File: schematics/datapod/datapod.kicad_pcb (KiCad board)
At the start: 2 copper layers, 152.7 x 152.7 mm, 56 parts, among them J1 Conn_01x02, J2 Conn_02x03_Odd_Even, J3 Conn_01x02, J4 DB9_Female, J5 DB9_Male_MountingHoles, J6 Micro_SD_Card, J7 Conn_02x02_Odd_Even, J8 Conn_01x02_Female, K1 DS2E-SL2-DC5V, K2 DS2E-SL2-DC5V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

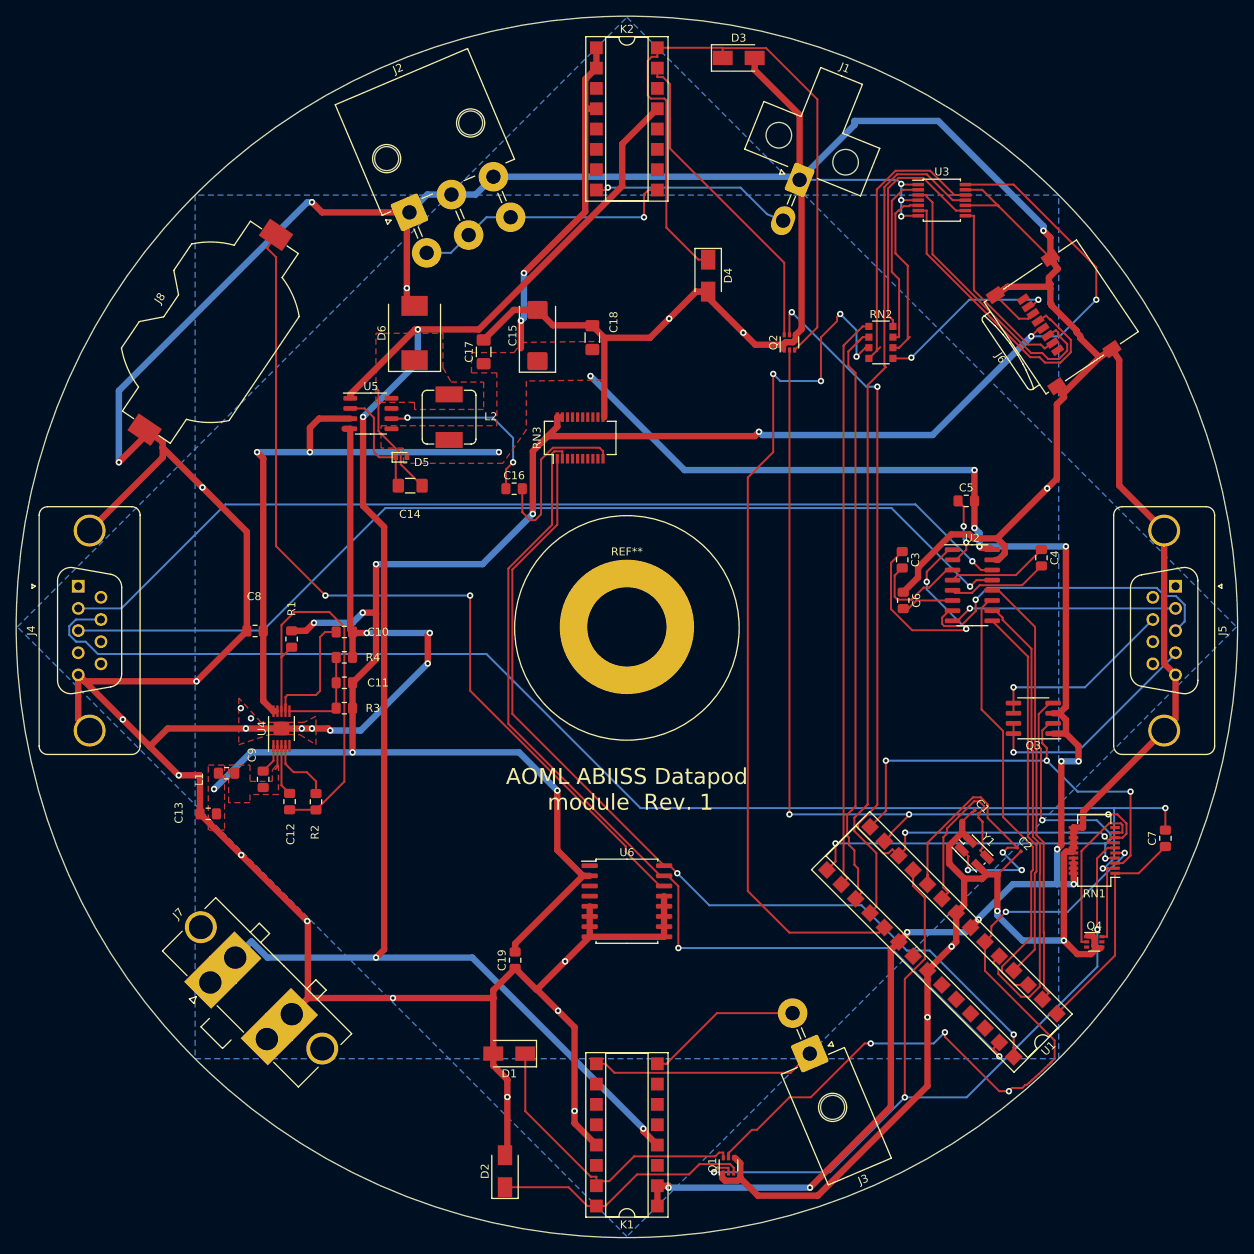
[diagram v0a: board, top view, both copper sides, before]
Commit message: restored lost changes... moving sd card reader and replacing rn2 with actual resistors
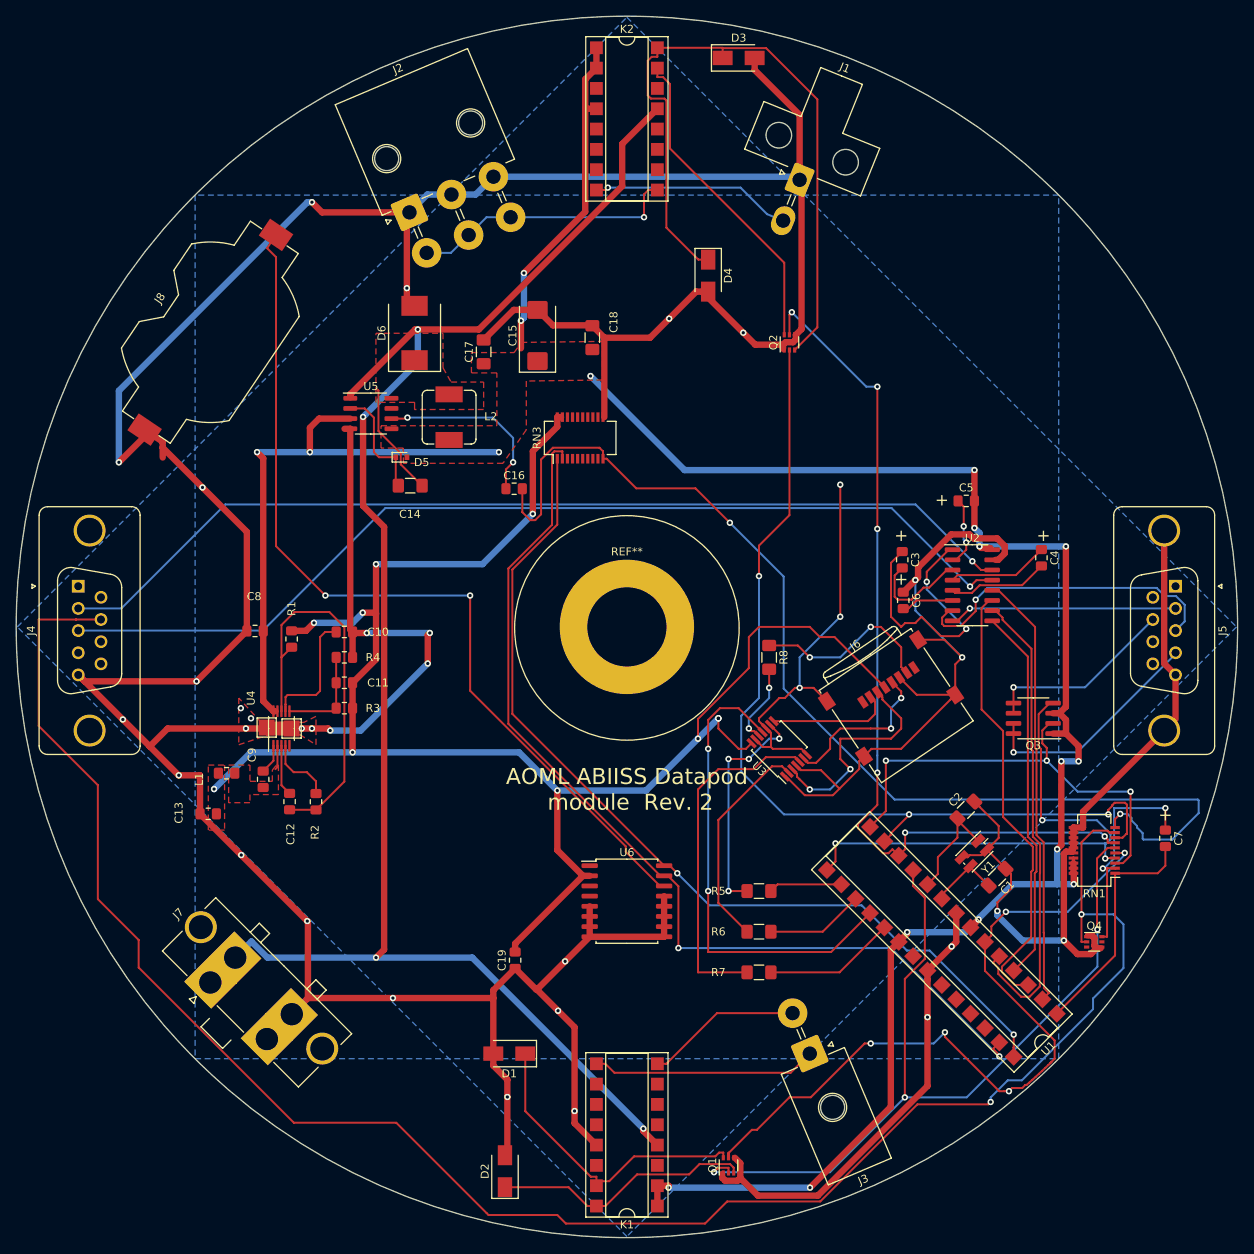
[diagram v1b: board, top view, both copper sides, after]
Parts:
- removed RN2: 3.3K, Resistor_SMD:R_Array_Convex_4x1206
- added R5: 3.3K, Resistor_SMD:R_1206_3216Metric_Pad1.42x1.75mm_HandSolder, F.Cu at (116.8, 129.5)
- added R6: 3.3K, Resistor_SMD:R_1206_3216Metric_Pad1.42x1.75mm_HandSolder, F.Cu at (116.8, 134.6)
- added R7: 3.3K, Resistor_SMD:R_1206_3216Metric_Pad1.42x1.75mm_HandSolder, F.Cu at (116.8, 139.7)
- added R8: 3.3K, Resistor_SMD:R_1206_3216Metric_Pad1.42x1.75mm_HandSolder, F.Cu at (118.1, 100.3)
- added REF**: TestPoint_Pad_2.0x2.0mm, TestPoint:TestPoint_Pad_2.0x2.0mm, F.Cu at (58.4, 109.2)
- added REF**: TestPoint_Pad_2.0x2.0mm, TestPoint:TestPoint_Pad_2.0x2.0mm, F.Cu at (55.3, 109.1)
- C1, C2: footprint Capacitor_SMD:C_0201_0603Metric -> Capacitor_SMD:C_1206_3216Metric_Pad1.42x1.75mm_HandSolder
- moved U3 71.5 mm to (119.4, 111.8), turned to 135 degrees
- moved J6 51.2 mm to (133.3, 105.4), turned to 34 degrees
- moved C1 8.53 mm to (146.6, 127.8), turned to 225 degrees
- moved C2 8.30 mm to (142.7, 119.4), turned to 45 degrees
- turned C7 to 270 degrees
- turned Y1 to 225 degrees
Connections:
- C7 pad 1: ~RESET -> DRAIN_PROG
- C7 pad 2: DRAIN_PROG -> ~RESET
- J4 pad 0: GND -> (no net)
- J4 pad 7: DRAIN_PROG -> RTS_PROG
- RN1 pad 10: Net-(RN1-Pad10) -> VcR1
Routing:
- net RTS_PROG: track 20.5 -> 236.4 mm, vias 0 -> 2
- net DRAIN_PROG: track 173.3 -> 28.2 mm
- net VcR1: track 22.3 -> 139.4 mm, vias 0 -> 2
- net MICRO_SD_SCK: track 109.4 -> 17.4 mm, vias 4 -> 0
- net GND: track 909.6 -> 820.7 mm
- net MICRO_SD_CS: track 72.6 -> 9.15 mm
- net MICRO_SD_MOSI: track 74.5 -> 12.3 mm
- net MICRO_SD_MISO: track 106.6 -> 59.9 mm, vias 0 -> 2
- net +3V3: track 247.6 -> 211.8 mm
- net Net-(R8-Pad2): track 36.1 -> 10.1 mm, vias 0 -> 2
- net Net-(C2-Pad1): track 38.6 -> 13.7 mm, vias 3 -> 0
- net Net-(R7-Pad1): track 22.3 -> 43.6 mm
- net Net-(J6-Pad5): track 37.7 -> 20.7 mm, vias 0 -> 2
- net Net-(C1-Pad2): track 23.8 -> 8.95 mm
- net Net-(J6-Pad2): track 24.1 -> 15.4 mm
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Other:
- board text added: "+"
- board text added: "AOML ABIISS Datapod module Rev. 2"
- board text removed: "AOML ABIISS Datapod module Rev. 1"

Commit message: fixed bad gnd trace on 3.3v circuit and added comments to the silkscreen
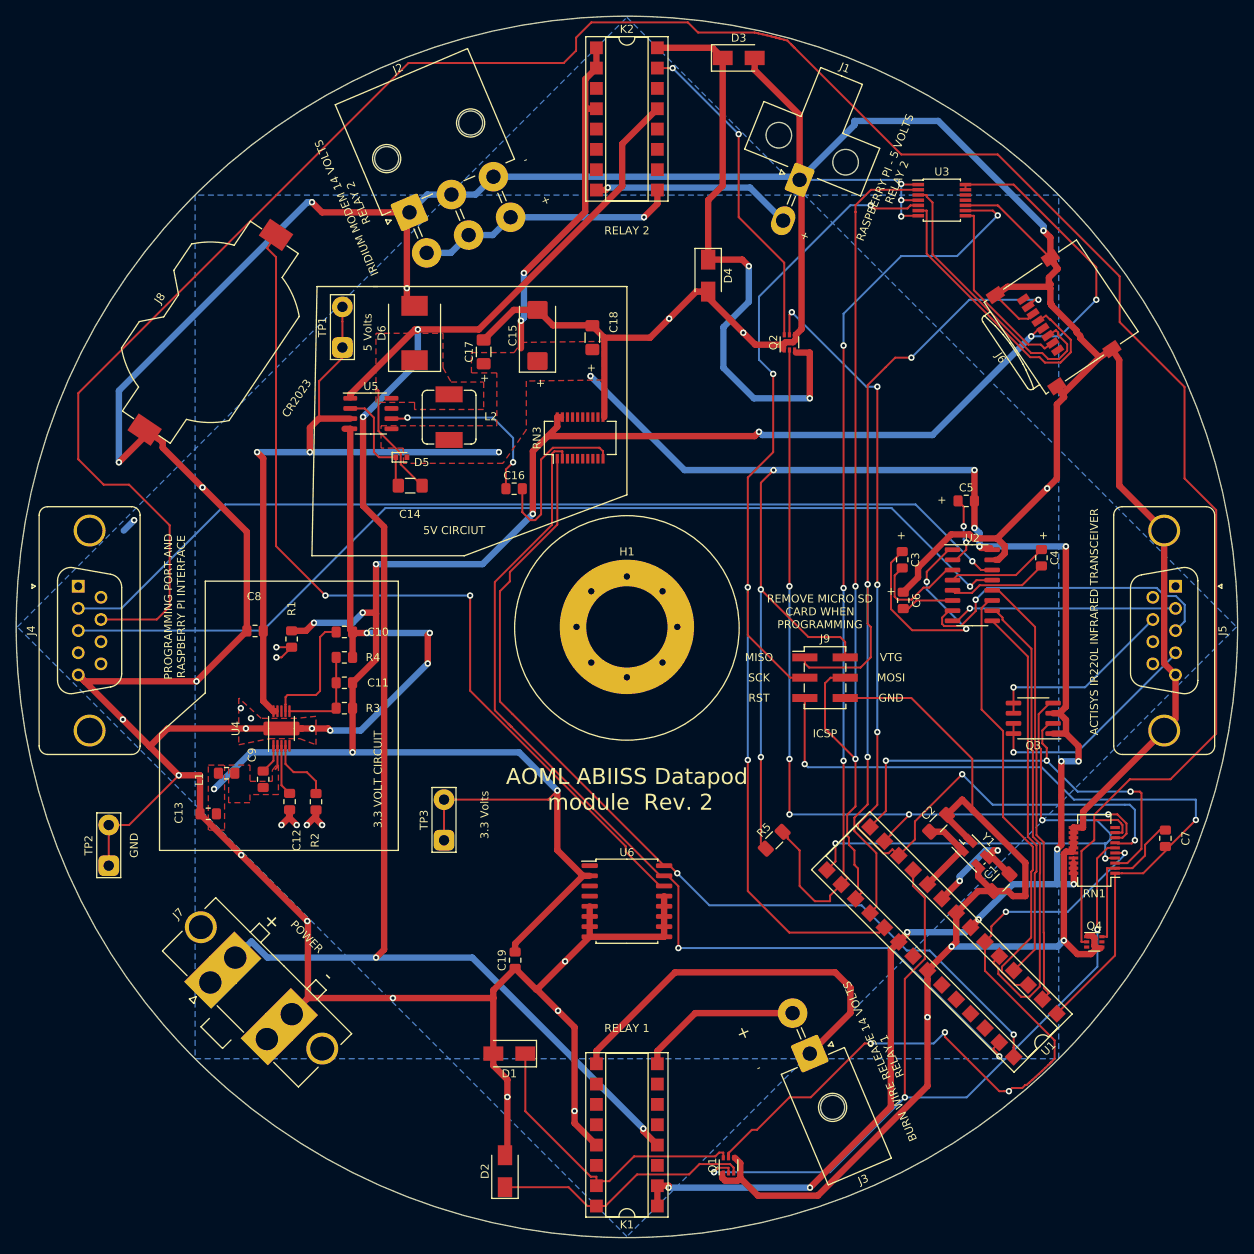
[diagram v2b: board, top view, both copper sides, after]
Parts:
- removed R6, R7, R8: 3.3K, Resistor_SMD:R_1206_3216Metric_Pad1.42x1.75mm_HandSolder
- removed REF** (x2): TestPoint_Pad_2.0x2.0mm, TestPoint:TestPoint_Pad_2.0x2.0mm
- removed REF**: MountingHole_8.4mm_M8_Pad, MountingHole:MountingHole_8.4mm_M8_Pad
- added G***: LOGO, datapod:noaa_logo, F.Cu at (43.8, 128.3)
- added H1: MountingHole, datapod:MountingHole_0.4_inches_Pad_Via, F.Cu at (100.3, 96.5)
- added J9: Conn_02x03_Odd_Even, Connector_PinHeader_2.54mm:PinHeader_2x03_P2.54mm_Vertical_SMD, F.Cu at (125.1, 102.9)
- added TP1: TestPoint_2Pole, TestPoint:TestPoint_2Pads_Pitch5.08mm_Drill1.3mm, F.Cu at (64.8, 61.6)
- added TP2: TestPoint_2Pole, TestPoint:TestPoint_2Pads_Pitch5.08mm_Drill1.3mm, F.Cu at (35.6, 126.4)
- added TP3: TestPoint_2Pole, TestPoint:TestPoint_2Pads_Pitch5.08mm_Drill1.3mm, F.Cu at (77.5, 123.2)
- R5: value 3.3K -> 10K
- moved U3 71.5 mm to (139.7, 43.2), turned to 0 degrees
- moved J6 51.2 mm to (153.7, 58.4), turned to 124 degrees
- moved R5 6.63 mm to (118.7, 123.2), turned to 45 degrees
- moved C2 3.80 mm to (139.3, 121.1)
- moved C1 0.85 mm to (147.1, 128.5), turned to 45 degrees
- turned Y1 to 315 degrees
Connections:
- C12 pad 2: Net-(C12-Pad2) -> GND
- J6 pad 7: Net-(J6-Pad7) -> MICRO_SD_MISO
- R1 pad 2: Net-(C12-Pad2) -> GND
- R2 pad 2: Net-(C12-Pad2) -> GND
- R5 pad 1: Net-(R5-Pad1) -> +5V
- RN1 pad 10: VcR1 -> Net-(RN1-Pad10)
- U3 pad 11: MICRO_SD_MISO -> Net-(U3-Pad11)
- U3 pad 13: GND -> +3V3
- U3 pad 2: Net-(R6-Pad1) -> MICRO_SD_MOSI
- U3 pad 5: Net-(R7-Pad1) -> MICRO_SD_SCK
- U3 pad 9: Net-(R5-Pad1) -> MICRO_SD_CS
- U4 pad 8: Net-(C12-Pad2) -> Net-(U4-Pad8)
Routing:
- net GND: track 820.7 -> 947.3 mm, vias 34 -> 39
- net MICRO_SD_SCK: track 17.4 -> 136.1 mm, vias 0 -> 4
- net VcR1: track 139.4 -> 22.3 mm, vias 2 -> 0
- net MICRO_SD_CS: track 9.15 -> 116.0 mm, vias 0 -> 4
- net MICRO_SD_MOSI: track 12.3 -> 111.3 mm, vias 0 -> 2
- net +5V: track 326.1 -> 404.7 mm, vias 18 -> 21
- net RTS_PROG: track 236.4 -> 311.2 mm, vias 2 -> 0
- net ~RESET: track 29.6 -> 95.3 mm, vias 0 -> 2
- net +3V3: track 211.8 -> 268.0 mm
- net MICRO_SD_MISO: track 59.9 -> 115.3 mm, vias 2 -> 4
- net Net-(C12-Pad2): track 49.5 -> 0.00 mm
- net Net-(R7-Pad1): track 43.6 -> 0.00 mm
- net Net-(R5-Pad1): track 28.5 -> 0.00 mm, vias 4 -> 0
- net Net-(R6-Pad1): track 27.4 -> 0.00 mm
- net Net-(J6-Pad7): track 23.2 -> 0.00 mm, vias 2 -> 0
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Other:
- board text added: "-"
- board text added: "3.3 VOLT CIRCUIT"
- board text added: "3.3 Volts"
- board text added: "5 Volts"
- board text added: "5V CIRCIUT"
- board text added: "ACTISYS IR220L INFRARED TRANSCEIVER"
- board text added: "BURN WIRE RELEASE 14 VOLTS RELAY 1"
- board text added: "CR2023"
- board text added: "GND"
- board text added: "ICSP"
- board text added: "IRIDIUM MODEM 14 VOLTS RELAY 2"
- board text added: "MISO"
- board text added: "MOSI"
- board text added: "POWER"
- board text added: "PROGRAMMING PORT AND RASPBERRY PI INTERFACE"
- board text added: "RASPBERRY PI - 5 VOLTS RELAY 2"
- board text added: "RELAY 1"
- board text added: "RELAY 2"
- board text added: "REMOVE MICRO SD CARD WHEN PROGRAMMING"
- board text added: "RST"
- board text added: "SCK"
- board text added: "VTG"

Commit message: added a jumper to select between 5v and 14v for the raspberry pi
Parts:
- removed G***: LOGO, datapod:noaa_logo
- added JP1: Jumper_3_Open, Jumper:SolderJumper-3_P1.3mm_Open_RoundedPad1.0x1.5mm, F.Cu at (89.5, 30.5)
- C1, C2: value 20pF -> 22pF
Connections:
- K2 pad 4: +5V -> Net-(JP1-Pad2)
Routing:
- net VCC: track 208.7 -> 234.3 mm
- net +5V: track 404.7 -> 416.2 mm, vias 21 -> 24
- net Net-(JP1-Pad2): track 0.00 -> 7.51 mm
- net GND: vias 39 -> 41
- net Net-(J1-Pad2): vias 1 -> 2
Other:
- board text added: "5V"
- board text added: "VCC"
